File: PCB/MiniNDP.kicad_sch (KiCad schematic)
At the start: 21 parts, among them J1 Conn_02x20_Odd_Even, U1 HC161, U2 HC161, U3 HC161, U4 HC138, U5 HC574, U6 AS6C4008, U7 1G32, U8 1G79

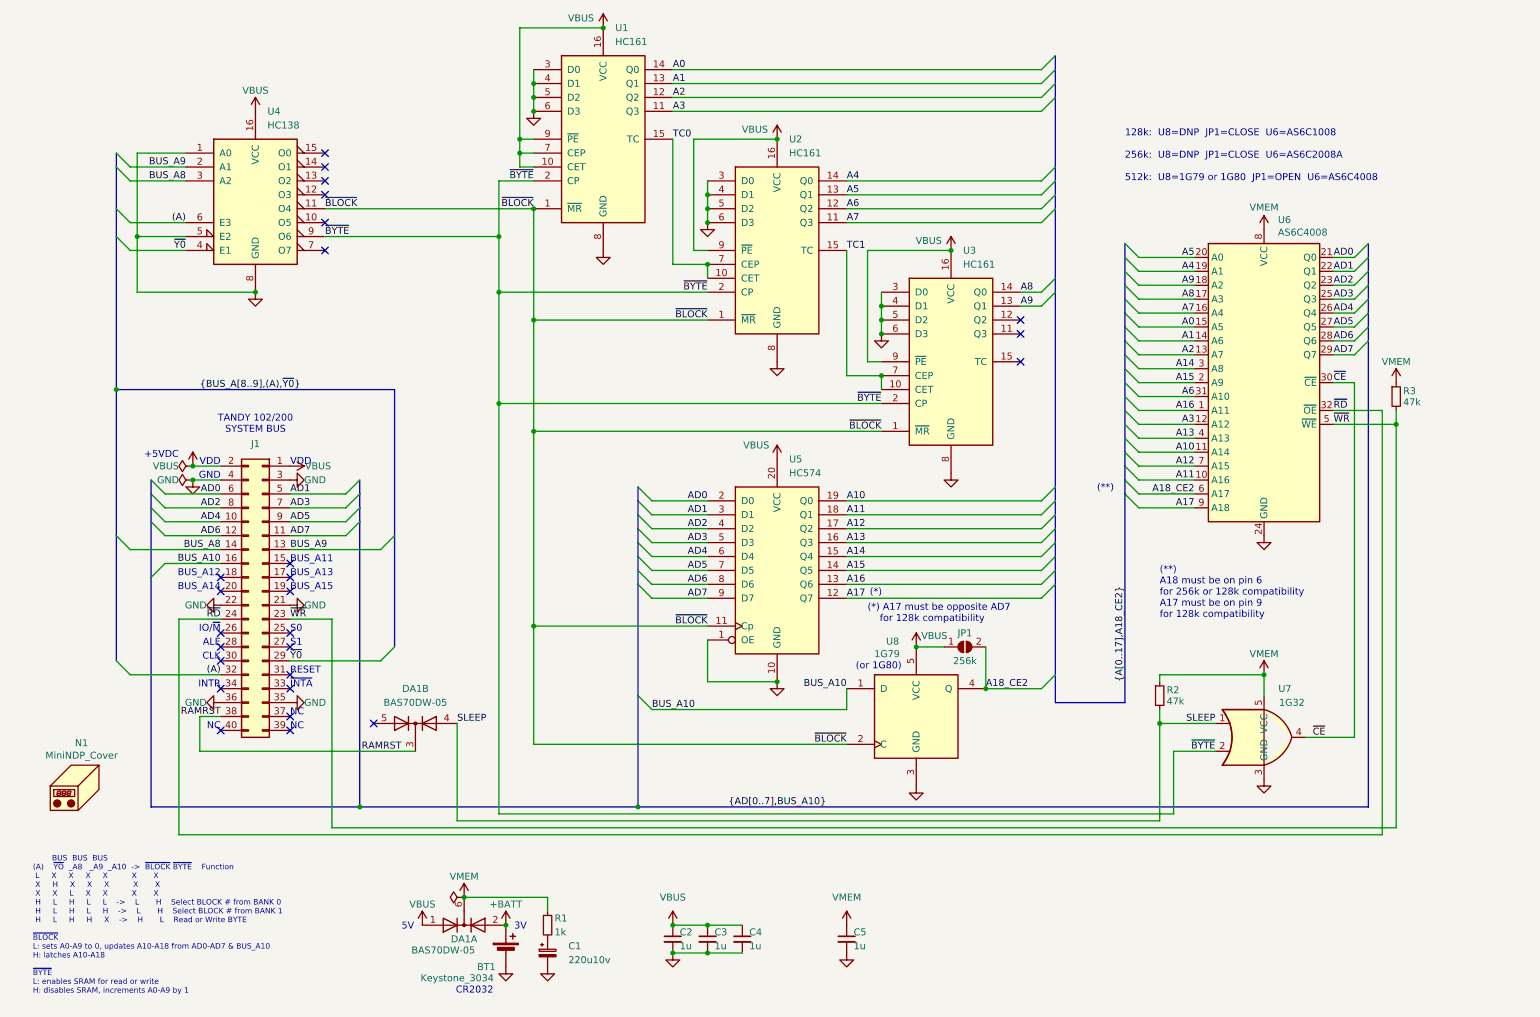
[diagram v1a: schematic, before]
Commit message: 1M_C 1 meg based on 4040
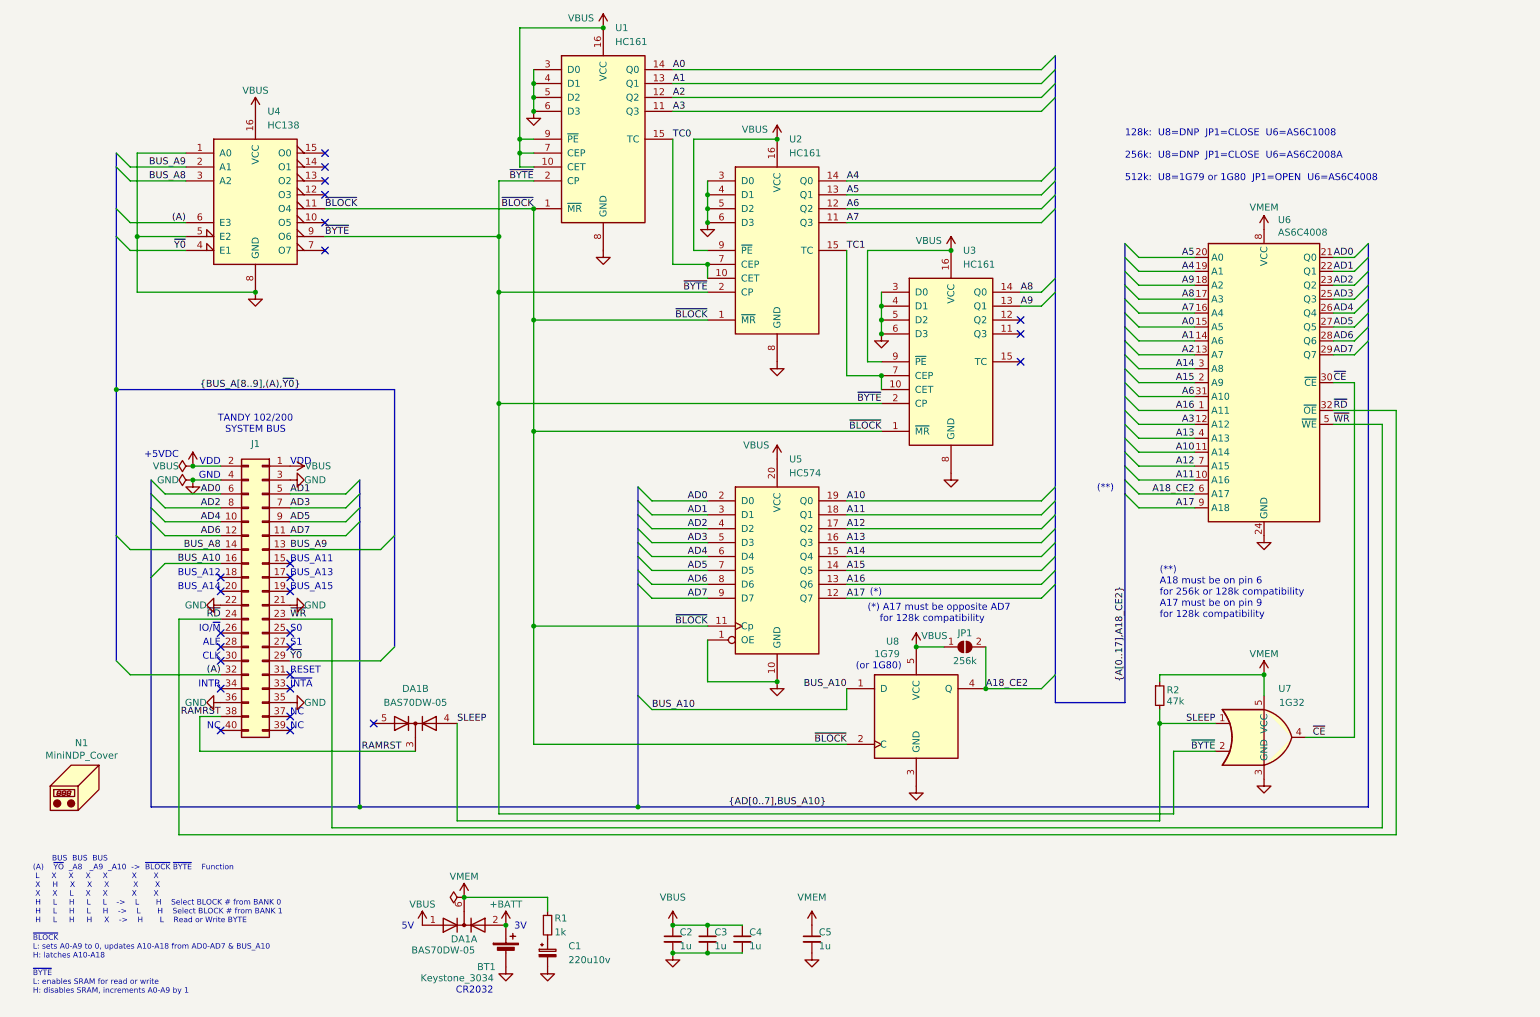
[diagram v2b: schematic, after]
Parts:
- removed R3: 47k, 000_LOCAL:R_0805, symbol 000_LOCAL:R
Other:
- moved on the sheet: C5
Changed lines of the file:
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@@
 	(title_block
 		(title "MiniNDP")
-		(date "2024-11-17")
-		(rev "E04")
+		(date "2024-11-26")
+		(rev "E05")
 		(company "Brian K. White - b.kenyon.w@gmail.com")
 		(comment 1 "github.com/bkw777/NODE_DATAPAC")
@@
 	)
 	(junction
-		(at 265.43 88.9)
-		(diameter 0)
-		(color 0 0 0 0)
-	)
-	(junction
 		(at 101.6 64.77)
 		(diameter 0)
@@
 	(wire
 		(pts
-			(xy 265.43 86.36) (xy 265.43 88.9)
-		)
-		(stroke
-			(width 0)
-			(type default)
-		)
-	)
-	(wire
-		(pts
 			(xy 222.25 143.51) (xy 222.25 161.29)
 		)
@@
 	(wire
 		(pts
-			(xy 265.43 88.9) (xy 265.43 162.56)
+			(xy 262.89 88.9) (xy 262.89 162.56)
 		)
 		(stroke
@@
 	(wire
 		(pts
-			(xy 254 88.9) (xy 265.43 88.9)
+			(xy 254 88.9) (xy 262.89 88.9)
 		)
 		(stroke
@@
 	(wire
 		(pts
-			(xy 265.43 162.56) (xy 71.12 162.56)
+			(xy 262.89 162.56) (xy 71.12 162.56)
 		)
 		(stroke
@@
 	(wire
 		(pts
-			(xy 254 86.36) (xy 262.89 86.36)
+			(xy 254 86.36) (xy 265.43 86.36)
 		)
 		(stroke
@@
 	(wire
 		(pts
-			(xy 262.89 163.83) (xy 262.89 86.36)
+			(xy 265.43 163.83) (xy 265.43 86.36)
 		)
 		(stroke
@@
 	(wire
 		(pts
-			(xy 43.18 163.83) (xy 262.89 163.83)
+			(xy 43.18 163.83) (xy 265.43 163.83)
 		)
 		(stroke
@@
 	(symbol
 		(lib_id "000_LOCAL:C")
-		(at 165.1 182.88 0)
+		(at 158.75 182.88 0)
 		(unit 1)
 		(exclude_from_sim no)
@@
 		(dnp no)
 		(property "Reference" "C5"
-			(at 166.37 181.61 0)
+			(at 160.02 181.61 0)
 			(effects
 				(font
@@
 		)
 		(property "Value" "1u"
-			(at 166.37 184.15 0)
+			(at 160.02 184.15 0)
 			(effects
 				(font
@@
 		)
 		(property "Footprint" "000_LOCAL:C_0805"
-			(at 166.0652 186.69 0)
+			(at 159.7152 186.69 0)
 			(effects
 				(font
@@
 		)
 		(property "Datasheet" "datasheets/CL21B105KAFNNNE.pdf"
-			(at 165.1 182.88 0)
+			(at 158.75 182.88 0)
 			(effects
 				(font
@@
 		)
 		(property "Description" "CAP CER 1UF 25V X7R 0805"
-			(at 165.1 182.88 0)
+			(at 158.75 182.88 0)
 			(effects
 				(font
@@
 		)
 		(property "MPN" "CL21B105KAFNNNE"
-			(at 165.1 182.88 0)
+			(at 158.75 182.88 0)
 			(effects
 				(font
@@
 	(symbol
 		(lib_id "power:VMEM")
-		(at 165.1 180.34 0)
+		(at 158.75 180.34 0)
 		(unit 1)
 		(exclude_from_sim no)
@@
 		(dnp no)
 		(property "Reference" "#PWR055"
-			(at 165.1 184.15 0)
+			(at 158.75 184.15 0)
 			(effects
 				(font
@@
 		)
 		(property "Value" "VMEM"
-			(at 165.1 175.26 0)
+			(at 158.75 175.26 0)
 			(effects
 				(font
@@
 		)
 		(property "Footprint" ""
-			(at 165.1 180.34 0)
+			(at 158.75 180.34 0)
 			(effects
 				(font
@@
 		)
 		(property "Datasheet" ""
-			(at 165.1 180.34 0)
+			(at 158.75 180.34 0)
 			(effects
 				(font
@@
 		)
 		(property "Description" ""
-			(at 165.1 180.34 0)
+			(at 158.75 180.34 0)
 			(effects
 				(font
@@
 	)
 	(symbol
-		(lib_id "000_LOCAL:R")
-		(at 265.43 83.82 0)
-		(unit 1)
-		(exclude_from_sim no)
-		(in_bom yes)
-		(on_board yes)
-		(dnp no)
-		(property "Reference" "R3"
-			(at 266.7 82.804 0)
-			(effects
-				(font
-					(size 1.27 1.27)
-				)
-				(justify left)
-			)
-		)
-		(property "Value" "47k"
-			(at 266.7 84.836 0)
-			(effects
-				(font
-					(size 1.27 1.27)
-				)
-				(justify left)
-			)
-		)
-		(property "Footprint" "000_LOCAL:R_0805"
-			(at 265.43 83.82 0)
-			(effects
-				(font
-					(size 1.27 1.27)
-				)
-				(hide yes)
-			)
-		)
-		(property "Datasheet" "datasheets/sei-rmcf_rmcp.pdf"
-			(at 265.43 83.82 0)
-			(effects
-				(font
-					(size 1.27 1.27)
-				)
-				(hide yes)
-			)
-		)
-		(property "Description" "RES 47K OHM 1% 1/8W 0805"
-			(at 265.43 83.82 0)
-			(effects
-				(font
-					(size 1.27 1.27)
-				)
-				(hide yes)
-			)
-		)
-		(property "MPN" "RMCF0805FT47K0"
-			(at 265.43 83.82 0)
-			(effects
-				(font
-					(size 1.27 1.27)
-				)
-				(hide yes)
-			)
-		)
-		(pin "1"
-		)
-		(pin "2"
-		)
-		(instances
-			(project "MiniNDP_512_E"
-				(path "/f15c2929-5cf4-4b4e-965d-148e1bec8a42"
-					(reference "R3")
-					(unit 1)
-				)
-			)
-		)
-	)
-	(symbol
 		(lib_id "power:GND")
 		(at 139.7 52.07 0)
@@
 	(symbol
 		(lib_id "power:VMEM")
-		(at 265.43 81.28 0)
-		(unit 1)
-		(exclude_from_sim no)
-		(in_bom yes)
-		(on_board yes)
-		(dnp no)
-		(property "Reference" "#PWR013"
-			(at 265.43 85.09 0)
-			(effects
-				(font
-					(size 1.27 1.27)
-				)
-				(hide yes)
-			)
-		)
-		(property "Value" "VMEM"
-			(at 265.43 77.47 0)
-			(effects
-				(font
-					(size 1.27 1.27)
-				)
-			)
-		)
-		(property "Footprint" ""
-			(at 265.43 81.28 0)
-			(effects
-				(font
-					(size 1.27 1.27)
-				)
-				(hide yes)
-			)
-		)
-		(property "Datasheet" ""
-			(at 265.43 81.28 0)
-			(effects
-				(font
-					(size 1.27 1.27)
-				)
-				(hide yes)
-			)
-		)
-		(property "Description" ""
-			(at 265.43 81.28 0)
-			(effects
-				(font
-					(size 1.27 1.27)
-				)
-				(hide yes)
-			)
-		)
-		(pin "1"
-		)
-		(instances
-			(project "MiniNDP_512"
-				(path "/f15c2929-5cf4-4b4e-965d-148e1bec8a42"
-					(reference "#PWR013")
-					(unit 1)
-				)
-			)
-		)
-	)
-	(symbol
-		(lib_id "power:VMEM")
 		(at 241.3 134.62 0)
 		(unit 1)
@@
 	(symbol
 		(lib_id "power:GND")
-		(at 165.1 185.42 0)
+		(at 158.75 185.42 0)
 		(unit 1)
 		(exclude_from_sim no)
@@
 		(dnp no)
 		(property "Reference" "#PWR041"
-			(at 165.1 191.77 0)
+			(at 158.75 191.77 0)
 			(effects
 				(font
@@
 		)
 		(property "Value" "GND"
-			(at 165.1 189.23 0)
+			(at 158.75 189.23 0)
 			(effects
 				(font
@@
 		)
 		(property "Footprint" ""
-			(at 165.1 185.42 0)
+			(at 158.75 185.42 0)
 			(effects
 				(font
@@
 		)
 		(property "Datasheet" ""
-			(at 165.1 185.42 0)
+			(at 158.75 185.42 0)
 			(effects
 				(font
@@
 		)
 		(property "Description" ""
-			(at 165.1 185.42 0)
+			(at 158.75 185.42 0)
 			(effects
 				(font

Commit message: easy boards add 47u cap, remove ramrst diode
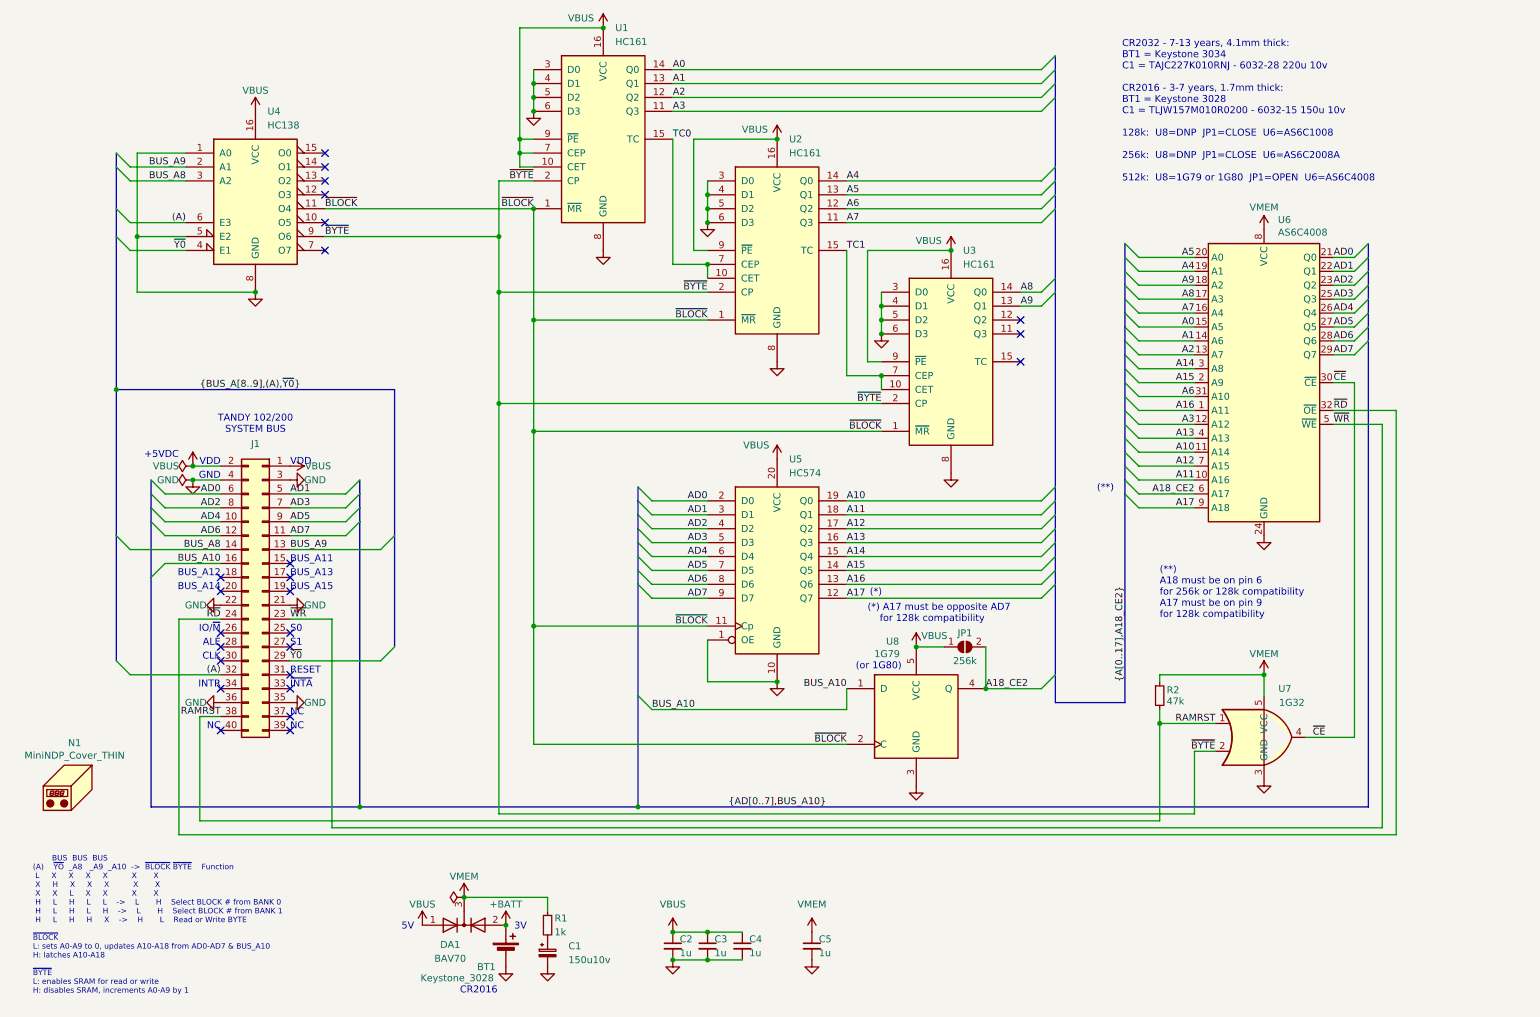
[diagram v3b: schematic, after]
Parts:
- removed DA1: BAS70DW-05, 000_LOCAL:SOT-363_SC-70-6_symmetric, symbol 000_LOCAL:BAV70S
- added DA1: BAV70, 000_LOCAL:SOT-23, symbol 000_LOCAL:BAV70
- BT1: value Keystone_3034 -> Keystone_3028; MPN Keystone 3034 -> Keystone_3028
- C1: value 220u10v -> 150u10v; MPN TAJC227K010RNJ -> TLJW157M010R0200
- N1: value MiniNDP_Cover -> MiniNDP_Cover_THIN; footprint 000_LOCAL:MiniNDP_Cover -> 000_LOCAL:MiniNDP_Cover_THIN; MPN MiniNDP_Cover.stl -> MiniNDP_Cover_THIN.stl
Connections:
- net SLEEP is gone; now on net RAMRST: R2.2, U7.1
- net +BATT: now also DA1.2 (A)
- net VBUS: now also DA1.1 (A)
- net VMEM: now also DA1.3 (K)
- no-connect marks 26 -> 25
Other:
- note added: "CR2016"
- note added: "CR2032 - 7-13 years, 4.1mm thick: BT1 = Keystone 3034 C1 = TAJC227K010RNJ - 6032-28 220u 10v CR2016 - 3-7 years, 1.7mm thick: BT1 = Keystone 3028 C1 = TLJW157M010R0200 - 6032-15 150u 10v 128k: U8=DNP JP1=CLOSE U6=AS6C1008 256k: U8=DNP JP1=CLOSE U6=AS6C2008A 512k: U8=1G79 or 1G80 JP1=OPEN U6=AS6C4008"
- note removed: "128k: U8=DNP JP1=CLOSE U6=AS6C1008 256k: U8=DNP JP1=CLOSE U6=AS6C2008A 512k: U8=1G79 or 1G80 JP1=OPEN U6=AS6C4008"
- note removed: "CR2032"
- moved on the sheet: C2, C3, C4, C5, N1
